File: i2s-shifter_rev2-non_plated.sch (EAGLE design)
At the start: 27 parts, among them IC1 74HC164D, IC2 74HC164D, IC3 74HC164D, IC4 74HC164D, IC5 74HC164D

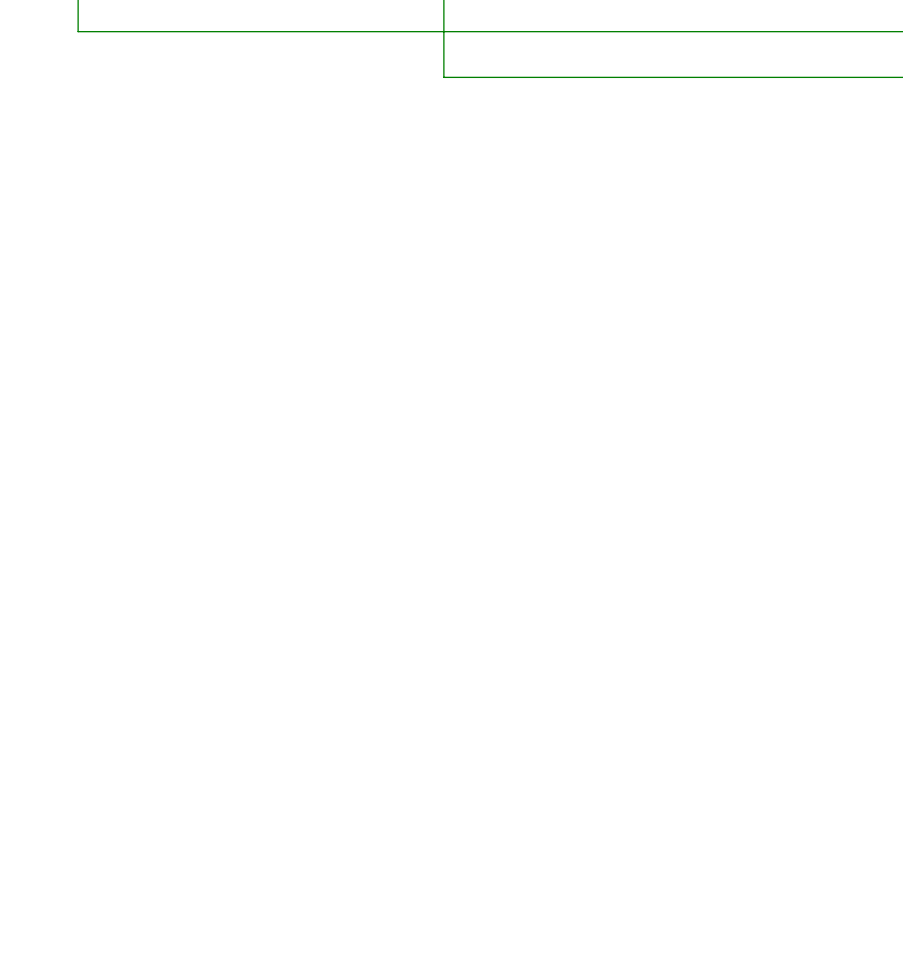
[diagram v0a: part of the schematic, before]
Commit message: wip dac board. added libs
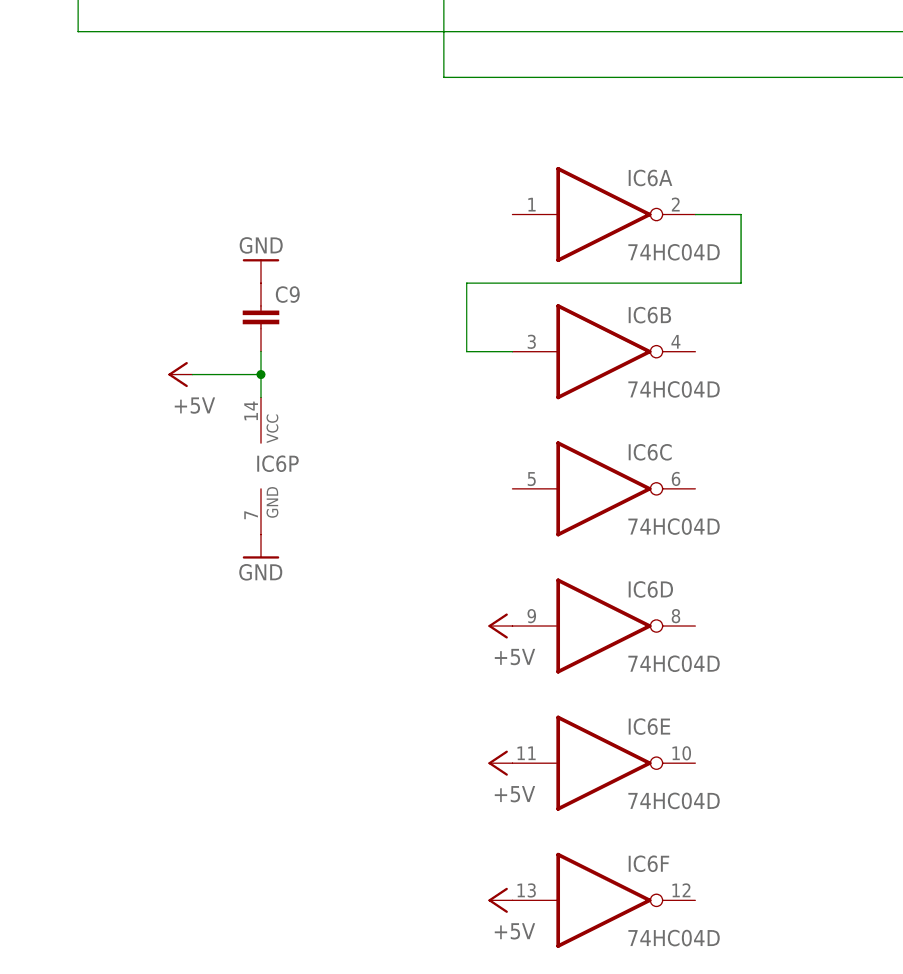
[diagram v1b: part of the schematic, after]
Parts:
- added C9: (no value), resistor:C-EU050-025X075
- added IC6: 74HC04D, 74xx-eu:74HC04D
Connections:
- new net +5V: C9.2, IC6D.I, IC6E.I, IC6F.I, IC6P.VCC
- new net N$9: IC6A.O, IC6B.I
- net GND: now also C9.1, IC6P.GND
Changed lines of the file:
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@@
 <?xml version="1.0" encoding="utf-8"?>
 <!DOCTYPE eagle SYSTEM "eagle.dtd">
-<eagle version="7.3.0">
+<eagle version="6.4">
 <drawing>
 <settings>
@@
 <grid distance="0.1" unitdist="inch" unit="inch" style="lines" multiple="1" display="no" altdistance="0.01" altunitdist="inch" altunit="inch"/>
 <layers>
-<layer number="1" name="Top" color="4" fill="1" visible="yes" active="no"/>
-<layer number="16" name="Bottom" color="1" fill="1" visible="yes" active="no"/>
-<layer number="17" name="Pads" color="2" fill="1" visible="yes" active="no"/>
-<layer number="18" name="Vias" color="2" fill="1" visible="yes" active="no"/>
-<layer number="19" name="Unrouted" color="6" fill="1" visible="yes" active="no"/>
-<layer number="20" name="Dimension" color="15" fill="1" visible="yes" active="no"/>
-<layer number="21" name="tPlace" color="7" fill="1" visible="yes" active="no"/>
-<layer number="22" name="bPlace" color="7" fill="1" visible="yes" active="no"/>
-<layer number="23" name="tOrigins" color="15" fill="1" visible="yes" active="no"/>
-<layer number="24" name="bOrigins" color="15" fill="1" visible="yes" active="no"/>
-<layer number="25" name="tNames" color="7" fill="1" visible="yes" active="no"/>
-<layer number="26" name="bNames" color="7" fill="1" visible="yes" active="no"/>
-<layer number="27" name="tValues" color="7" fill="1" visible="yes" active="no"/>
-<layer number="28" name="bValues" color="7" fill="1" visible="yes" active="no"/>
+<layer number="1" name="Top" color="4" fill="1" visible="no" active="no"/>
+<layer number="16" name="Bottom" color="1" fill="1" visible="no" active="no"/>
+<layer number="17" name="Pads" color="2" fill="1" visible="no" active="no"/>
+<layer number="18" name="Vias" color="2" fill="1" visible="no" active="no"/>
+<layer number="19" name="Unrouted" color="6" fill="1" visible="no" active="no"/>
+<layer number="20" name="Dimension" color="15" fill="1" visible="no" active="no"/>
+<layer number="21" name="tPlace" color="7" fill="1" visible="no" active="no"/>
+<layer number="22" name="bPlace" color="7" fill="1" visible="no" active="no"/>
+<layer number="23" name="tOrigins" color="15" fill="1" visible="no" active="no"/>
+<layer number="24" name="bOrigins" color="15" fill="1" visible="no" active="no"/>
+<layer number="25" name="tNames" color="7" fill="1" visible="no" active="no"/>
+<layer number="26" name="bNames" color="7" fill="1" visible="no" active="no"/>
+<layer number="27" name="tValues" color="7" fill="1" visible="no" active="no"/>
+<layer number="28" name="bValues" color="7" fill="1" visible="no" active="no"/>
 <layer number="29" name="tStop" color="7" fill="3" visible="no" active="no"/>
 <layer number="30" name="bStop" color="7" fill="6" visible="no" active="no"/>
@@
 <layer number="35" name="tGlue" color="7" fill="4" visible="no" active="no"/>
 <layer number="36" name="bGlue" color="7" fill="5" visible="no" active="no"/>
-<layer number="37" name="tTest" color="7" fill="1" visible="yes" active="no"/>
-<layer number="38" name="bTest" color="7" fill="1" visible="yes" active="no"/>
+<layer number="37" name="tTest" color="7" fill="1" visible="no" active="no"/>
+<layer number="38" name="bTest" color="7" fill="1" visible="no" active="no"/>
 <layer number="39" name="tKeepout" color="4" fill="11" visible="no" active="no"/>
 <layer number="40" name="bKeepout" color="1" fill="11" visible="no" active="no"/>
@@
 <layer number="44" name="Drills" color="7" fill="1" visible="no" active="no"/>
 <layer number="45" name="Holes" color="7" fill="1" visible="no" active="no"/>
-<layer number="46" name="Milling" color="3" fill="1" visible="yes" active="no"/>
-<layer number="47" name="Measures" color="7" fill="1" visible="yes" active="no"/>
-<layer number="48" name="Document" color="7" fill="1" visible="yes" active="no"/>
-<layer number="49" name="Reference" color="7" fill="1" visible="yes" active="no"/>
-<layer number="51" name="tDocu" color="7" fill="1" visible="yes" active="no"/>
-<layer number="52" name="bDocu" color="7" fill="1" visible="yes" active="no"/>
+<layer number="46" name="Milling" color="3" fill="1" visible="no" active="no"/>
+<layer number="47" name="Measures" color="7" fill="1" visible="no" active="no"/>
+<layer number="48" name="Document" color="7" fill="1" visible="no" active="no"/>
+<layer number="49" name="Reference" color="7" fill="1" visible="no" active="no"/>
+<layer number="51" name="tDocu" color="7" fill="1" visible="no" active="no"/>
+<layer number="52" name="bDocu" color="7" fill="1" visible="no" active="no"/>
 <layer number="91" name="Nets" color="2" fill="1" visible="yes" active="yes"/>
 <layer number="92" name="Busses" color="1" fill="1" visible="yes" active="yes"/>
@@
 <part name="GND19" library="supply1" deviceset="GND" device=""/>
 <part name="GND20" library="supply1" deviceset="GND" device=""/>
+<part name="IC6" library="74xx-eu" deviceset="74*04" device="D" technology="HC"/>
+<part name="C9" library="resistor" deviceset="C-EU" device="050-025X075"/>
+<part name="P+3" library="supply1" deviceset="+5V" device=""/>
+<part name="GND21" library="supply1" deviceset="GND" device=""/>
+<part name="GND22" library="supply1" deviceset="GND" device=""/>
+<part name="P+4" library="supply1" deviceset="+5V" device=""/>
+<part name="P+5" library="supply1" deviceset="+5V" device=""/>
+<part name="P+6" library="supply1" deviceset="+5V" device=""/>
 </parts>
 <sheets>
@@
 <instance part="GND19" gate="1" x="-10.16" y="66.04" rot="R90"/>
 <instance part="GND20" gate="1" x="-10.16" y="58.42" rot="R90"/>
+<instance part="IC6" gate="A" x="58.42" y="-5.08"/>
+<instance part="IC6" gate="B" x="58.42" y="-20.32"/>
+<instance part="IC6" gate="C" x="58.42" y="-35.56"/>
+<instance part="IC6" gate="D" x="58.42" y="-50.8"/>
+<instance part="IC6" gate="E" x="58.42" y="-66.04"/>
+<instance part="IC6" gate="P" x="20.32" y="-33.02"/>
+<instance part="IC6" gate="F" x="58.42" y="-81.28"/>
+<instance part="C9" gate="G$1" x="20.32" y="-15.24"/>
+<instance part="P+3" gate="1" x="10.16" y="-22.86" rot="R90"/>
+<instance part="GND21" gate="1" x="20.32" y="-10.16" rot="R180"/>
+<instance part="GND22" gate="1" x="20.32" y="-43.18"/>
+<instance part="P+4" gate="1" x="45.72" y="-81.28" rot="R90"/>
+<instance part="P+5" gate="1" x="45.72" y="-66.04" rot="R90"/>
+<instance part="P+6" gate="1" x="45.72" y="-50.8" rot="R90"/>
 </instances>
 <busses>
@@
 <pinref part="GND20" gate="1" pin="GND"/>
 </segment>
-</net>
+<segment>
+<pinref part="C9" gate="G$1" pin="1"/>
+<pinref part="GND21" gate="1" pin="GND"/>
+</segment>
+<segment>
+<pinref part="IC6" gate="P" pin="GND"/>
+<pinref part="GND22" gate="1" pin="GND"/>
+</segment>
+</net>
+<net name="+5V" class="0">
+<segment>
+<pinref part="C9" gate="G$1" pin="2"/>
+<pinref part="IC6" gate="P" pin="VCC"/>
+<wire x1="20.32" y1="-20.32" x2="20.32" y2="-22.86" width="0.1524" layer="91"/>
+<pinref part="P+3" gate="1" pin="+5V"/>
+<wire x1="20.32" y1="-22.86" x2="20.32" y2="-25.4" width="0.1524" layer="91"/>
+<wire x1="20.32" y1="-22.86" x2="12.7" y2="-22.86" width="0.1524" layer="91"/>
+<junction x="20.32" y="-22.86"/>
+</segment>
+<segment>
+<pinref part="IC6" gate="F" pin="I"/>
+<pinref part="P+4" gate="1" pin="+5V"/>
+</segment>
+<segment>
+<pinref part="IC6" gate="E" pin="I"/>
+<pinref part="P+5" gate="1" pin="+5V"/>
+</segment>
+<segment>
+<pinref part="IC6" gate="D" pin="I"/>
+<pinref part="P+6" gate="1" pin="+5V"/>
+</segment>
+</net>
+<net name="N$9" class="0">
+<segment>
+<pinref part="IC6" gate="A" pin="O"/>
+<wire x1="68.58" y1="-5.08" x2="73.66" y2="-5.08" width="0.1524" layer="91"/>
+<wire x1="73.66" y1="-5.08" x2="73.66" y2="-12.7" width="0.1524" layer="91"/>
+<wire x1="73.66" y1="-12.7" x2="43.18" y2="-12.7" width="0.1524" layer="91"/>
+<wire x1="43.18" y1="-12.7" x2="43.18" y2="-20.32" width="0.1524" layer="91"/>
+<pinref part="IC6" gate="B" pin="I"/>
+<wire x1="43.18" y1="-20.32" x2="48.26" y2="-20.32" width="0.1524" layer="91"/>
+</segment>
+</net>
